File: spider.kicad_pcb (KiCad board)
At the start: 2 copper layers, 22.7 x 30.2 mm, 19 parts, among them IC1 ATMEGA88-A, J1 CONN_02X04, P2 USB_OTG, P3 CONN_01X01, U1 ESP8266-ESP-03, U2 nRF24L01+, U3 LD1117S33TR, U4 HS0038

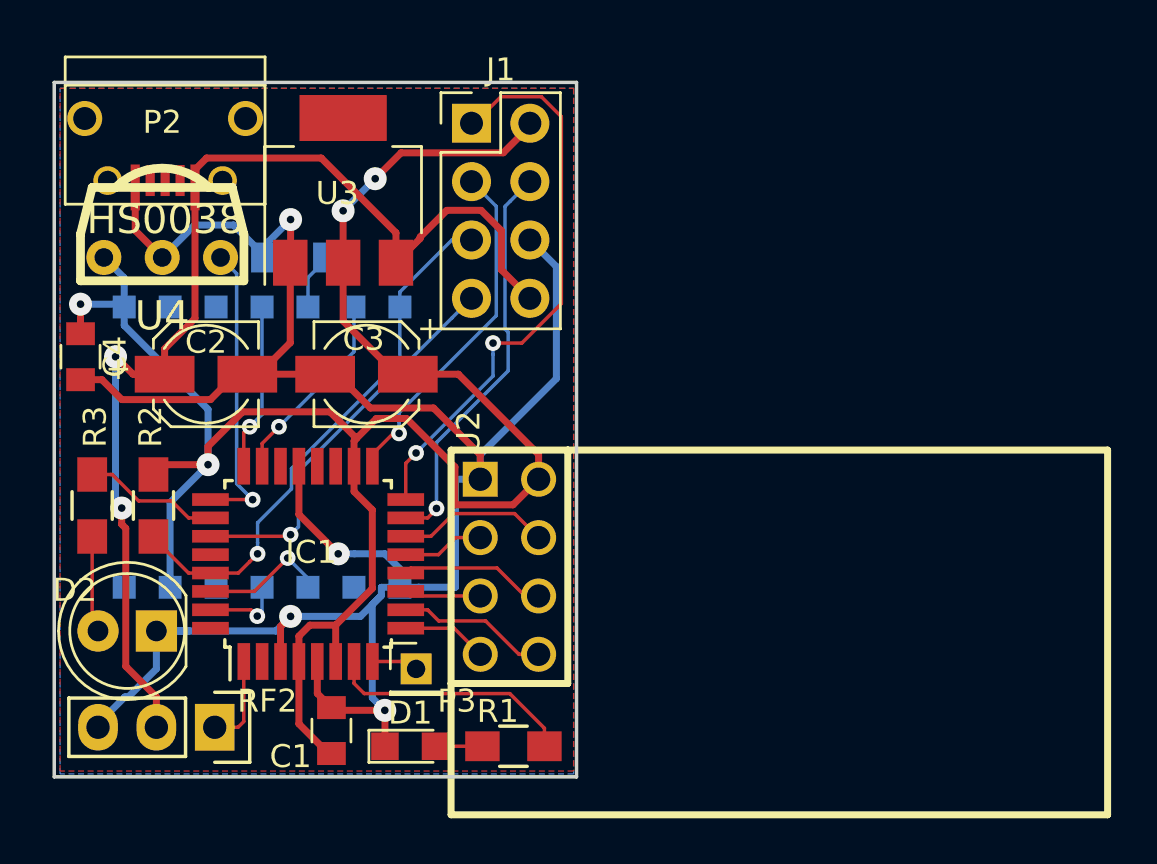
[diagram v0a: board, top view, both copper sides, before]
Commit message: Add more expansion pins, route 5V to transmitter, add small fixes.
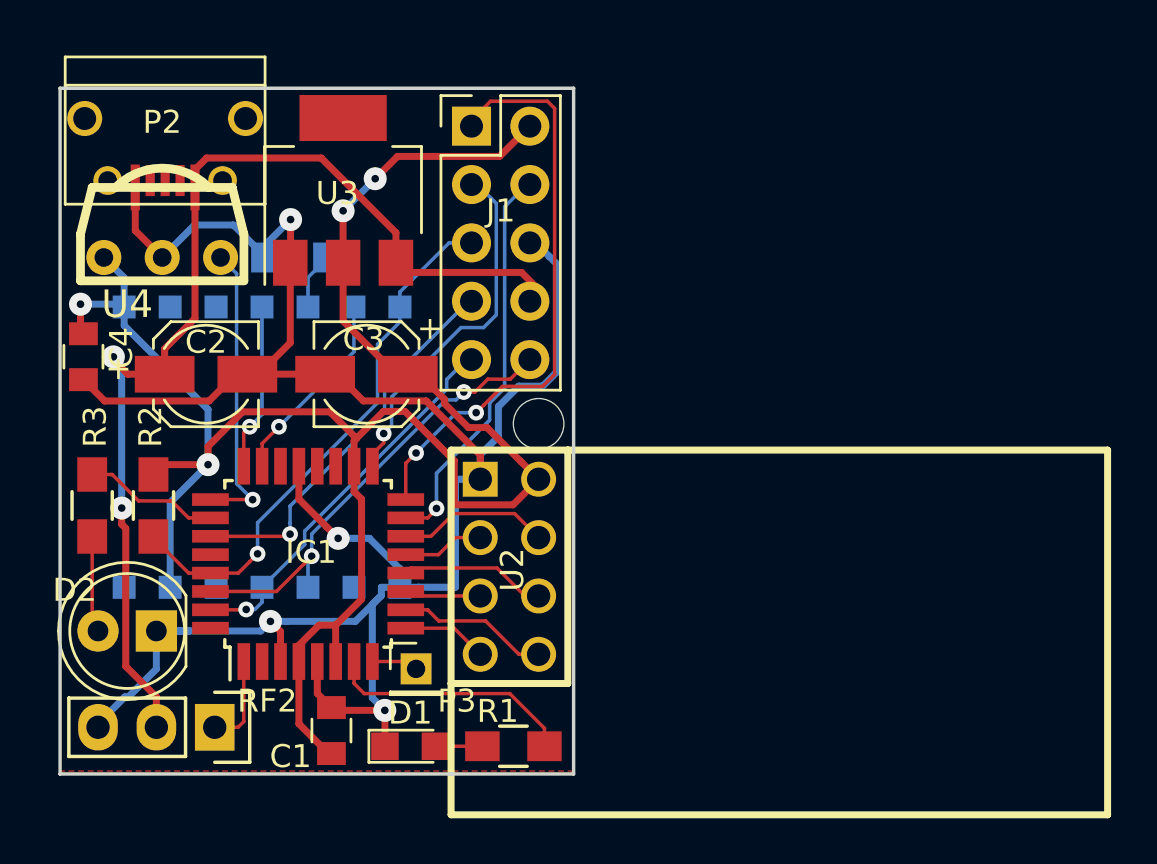
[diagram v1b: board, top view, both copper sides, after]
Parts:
- added REF**: MountingHole_2.2mm_M2, Mounting_Holes:MountingHole_2.2mm_M2, F.Cu at (140.8, 120.3)
- added © 2017 CC BY-SA: Danny Havenith, spider:oshardware, B.Cu at (133.0, 109.2)
- J1: value CONN_02X04 -> CONN_02X05; footprint Pin_Headers:Pin_Header_Straight_2x04_Pitch2.54mm -> Pin_Headers:Pin_Header_Straight_2x05_Pitch2.54mm
- RF2: value RF_Transmitter_433_MHz -> 433 MHz
- moved C4 0.13 mm to (121.0, 117.3)
- moved J1 0.13 mm to (137.9, 107.3)
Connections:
- IC1 pad 30: Net-(IC1-Pad30) -> /espTX
- IC1 pad 31: Net-(IC1-Pad31) -> /expRX
- U1 pad 3: Net-(IC1-Pad30) -> /espTX
- U1 pad 4: Net-(IC1-Pad31) -> /expRX
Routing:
- net /espTX: track 0.00 -> 20.1 mm, vias 0 -> 2
- net /expRX: track 0.00 -> 17.5 mm, vias 0 -> 1
- net Net-(IC1-Pad30): track 5.60 -> 0.00 mm, vias 1 -> 0
- net Net-(IC1-Pad31): track 3.71 -> 0.00 mm, vias 1 -> 0
- net /5V: track 50.1 -> 47.8 mm
- net VCC: track 87.1 -> 86.4 mm
- net /SCK: track 15.2 -> 15.8 mm
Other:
- board size 22.7 x 30.2 mm -> 22.4 x 29.8 mm

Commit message: Clean up component files.
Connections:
- net /expRX renamed /espRX
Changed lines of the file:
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@@
     (mod_text_size 1 1)
     (mod_text_width 0.15)
-    (pad_size 1.25 1.25)
-    (pad_drill 0.8128)
+    (pad_size 1.35 0.4)
+    (pad_drill 0)
     (pad_to_mask_clearance 0.2)
     (aux_axis_origin 0 0)
@@
   (net 38 /ADCin)
   (net 39 /espTX)
-  (net 40 /expRX)
+  (net 40 /espRX)
   (net_class Default "This is the default net class."
     (clearance 0.1524)
@@
     (add_net /SCK)
     (add_net /SCKnRF)
+    (add_net /espRX)
     (add_net /espTX)
-    (add_net /expRX)
     (add_net /int0)
     (add_net /int1)
@@
     (descr "Micro USB Type B Receptacle")
     (tags "USB USB_B USB_micro USB_OTG")
+    (clearance 0.12)
     (attr smd)
     (fp_text reference P2 (at 0.127 1.19 180) (layer F.SilkS)
@@
     (fp_line (start -4.35 4.03) (end -4.35 -2.38) (layer F.SilkS) (width 0.12))
     (pad 1 smd rect (at -1.3 -1.65 270) (size 2 0.4) (layers F.Cu F.Paste F.Mask)
-      (net 23 /5V))
+      (net 23 /5V) (solder_mask_margin 0.12))
     (pad 2 smd rect (at -0.65 -1.35 270) (size 1.35 0.4) (layers F.Cu F.Paste)
       (net 18 "Net-(P2-Pad2)"))
     (pad 3 smd rect (at 0 -1.35 270) (size 1.35 0.4) (layers F.Cu F.Paste F.Mask)
-      (net 19 "Net-(P2-Pad3)"))
+      (net 19 "Net-(P2-Pad3)") (solder_mask_margin 0.12))
     (pad 4 smd rect (at 0.65 -1.35 270) (size 1.35 0.4) (layers F.Cu F.Paste)
       (net 20 "Net-(P2-Pad4)"))
     (pad 5 smd rect (at 1.3 -1.65 270) (size 2 0.4) (layers F.Cu F.Paste F.Mask)
-      (net 6 GND))
+      (net 6 GND) (solder_mask_margin 0.12))
     (pad 6 thru_hole oval (at -2.5 -1.35 270) (size 1.25 1.25) (drill 0.8128) (layers *.Cu *.Mask)
       (net 21 "Net-(P2-Pad6)"))
@@
       (net 23 /5V))
     (pad 9 thru_hole oval (at 0 10.16) (size 1.7 1.7) (drill 1) (layers *.Cu *.Mask)
-      (net 40 /expRX))
+      (net 40 /espRX))
     (pad 10 thru_hole oval (at 2.54 10.16) (size 1.7 1.7) (drill 1) (layers *.Cu *.Mask)
       (net 39 /espTX))
@@
       (net 39 /espTX))
     (pad 4 smd rect (at 6.1 0.1 270) (size 1 1) (layers B.Cu B.Paste B.Mask)
-      (net 40 /expRX))
+      (net 40 /espRX))
     (pad 5 smd rect (at 6.1 2.1 270) (size 1 1) (layers B.Cu B.Paste B.Mask)
       (net 3 "Net-(U1-Pad5)"))
@@
       (net 39 /espTX))
     (pad 31 smd rect (at -2 -4.25 180) (size 1.6 0.55) (layers F.Cu F.Paste F.Mask)
-      (net 40 /expRX))
+      (net 40 /espRX))
     (pad 32 smd rect (at -2.8 -4.25 180) (size 1.6 0.55) (layers F.Cu F.Paste F.Mask)
       (net 22 "Net-(IC1-Pad32)"))
